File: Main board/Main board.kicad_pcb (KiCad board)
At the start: 4 copper layers, 230.2 x 100.5 mm, 80 parts, among them CN1 PA001-4P, CN2 PA001-4P, J1 TagConnect_TC2030-NL, J2 Conn_01x02_Pin, J3 Conn_01x02_Pin, J5 Connector, USB-TYPE-C-16P, J6 436500201, J7 Conn_01x04_Pin, Q1 SI7232DN-T1-GE3, Q2 SI7232DN-T1-GE3, SW1 SKRKAEE020, SW2 SKRKAEE020, U1 STM32U575VGTx, U2 TPS62901RPJR, U3 MS5607-02BA03, U4 ADXL375BCCZ-RL7, U5 SN74LVC1G32MDBVREP, U6 MMC5983MA, U9 ICM-45686, X1 1XXD32000MBA

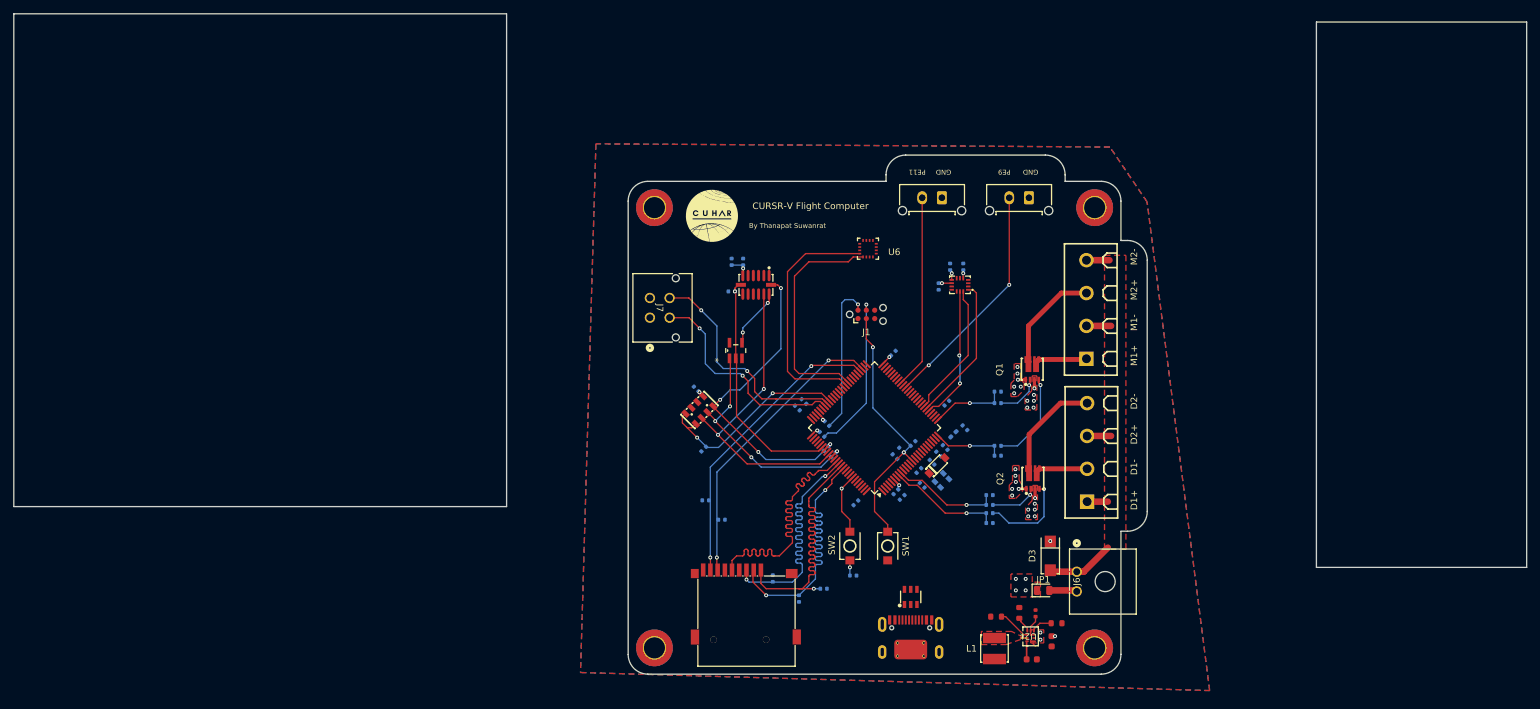
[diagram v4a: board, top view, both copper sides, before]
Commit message: Final Layout (Pre-silkscreen)
- Added  1M resistors in parallel with the igniters for static dissipation
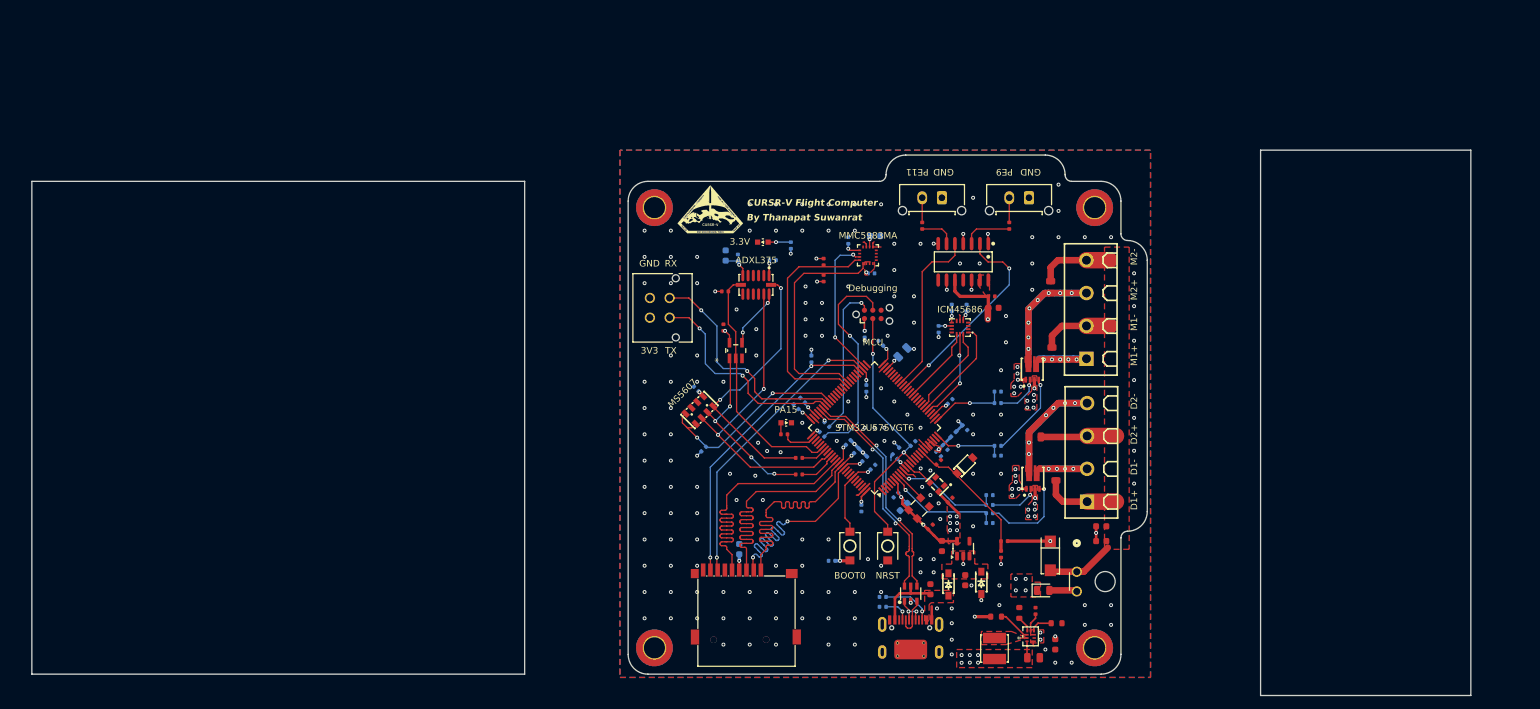
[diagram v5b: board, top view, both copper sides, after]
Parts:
- removed the G*** at (125.2, 67.8)
- added C15: 100nF, PCM_JLCPCB:C_0402, F.Cu at (167.8, 80.0)
- added C16: 100nF, PCM_JLCPCB:C_0402, B.Cu at (134.5, 74.5)
- added C22: 100nF, PCM_JLCPCB:C_0402, F.Cu at (127.0, 84.8)
- added C23: 1uF, PCM_JLCPCB:C_0402, B.Cu at (146.0, 71.5)
- added C24: 10uF, PCM_JLCPCB:C_0603, B.Cu at (150.1, 70.8)
- added C25: 10uF, PCM_JLCPCB:C_0603, F.Cu at (168.1, 81.8)
- added C26: 10uF, PCM_JLCPCB:C_0603, F.Cu at (158.5, 124.6)
- added C31: 10uF, PCM_JLCPCB:C_0603, F.Cu at (184.5, 117.2)
- added C32: 100nF, PCM_JLCPCB:C_0603, F.Cu at (184.5, 115.0)
- added C34: 4.7uF, PCM_JLCPCB:C_0805, B.Cu at (154.3, 88.5)
- added C35: 10uF, PCM_JLCPCB:C_0603, F.Cu at (160.2, 118.0)
- added C36: 10uF, PCM_JLCPCB:C_0603, F.Cu at (163.8, 123.2)
- added C37: 100nF, PCM_JLCPCB:C_0603, B.Cu at (129.4, 118.5)
- added C38: 100nF, PCM_JLCPCB:C_0402, B.Cu at (149.5, 76.5)
- added D4: GREEN, LEDDD:WL-SMCW_0603, F.Cu at (133.0, 71.8)
- added D5: Blue, LEDDD:WL-SMCW_0603, F.Cu at (136.6, 99.2)
- added G***: LOGO, LOGO, F.Cu at (125.0, 66.8)
- added G***: LOGO, LOGO, B.Cu at (133.8, 67.5)
- added G***: LOGO, LOGO, B.Cu at (145.5, 66.8)
- added G***: LOGO, LOGO, B.Cu at (124.8, 67.5)
- added R17: 4.7kΩ, PCM_JLCPCB:R_0402, F.Cu at (142.2, 77.2)
- added R18: 4.7kΩ, PCM_JLCPCB:R_0402, F.Cu at (142.2, 74.8)
- added R19: 10kΩ, PCM_JLCPCB:R_0402, B.Cu at (149.8, 106.0)
- added R20: 100Ω, PCM_JLCPCB:R_0402, B.Cu at (148.5, 85.8)
- added R21: 470Ω, PCM_JLCPCB:R_0402, B.Cu at (137.3, 72.2)
- added R22: 5.1kΩ, PCM_JLCPCB:R_0402, B.Cu at (151.2, 127.2)
- added R23: 5.1kΩ, PCM_JLCPCB:R_0402, B.Cu at (151.2, 125.8)
- added R27: 47kΩ, PCM_JLCPCB:R_0402, F.Cu at (169.8, 117.2)
- added R28: 27kΩ, PCM_JLCPCB:R_0402, F.Cu at (169.2, 119.2)
- added R39: 470Ω, PCM_JLCPCB:R_0402, F.Cu at (136.2, 101.0)
- added R40: 1MΩ, PCM_JLCPCB:R_0805, F.Cu at (176.8, 78.6)
- added R41: 1MΩ, PCM_JLCPCB:R_0805, F.Cu at (177.0, 88.7)
- added R42: 1MΩ, PCM_JLCPCB:R_0805, F.Cu at (177.6, 107.1)
- added R43: 1MΩ, PCM_JLCPCB:R_0805, F.Cu at (174.4, 101.4)
- added R5: 75Ω, PCM_JLCPCB:R_0402, F.Cu at (170.5, 69.2)
- added R8: 75Ω, PCM_JLCPCB:R_0402, F.Cu at (157.2, 69.2)
- added U10: TLV75733PDBV, Package_TO_SOT_SMD:SOT-23-5, F.Cu at (163.5, 118.4)
- added U11: NRVB120VLSFT1G, EASYEDA:SOD-123_L2.7-W1.6-LS3.7-RD-1, F.Cu at (161.2, 123.8)
- added U12: NRVB120VLSFT1G, EASYEDA:SOD-123_L2.7-W1.6-LS3.7-RD-1, F.Cu at (166.2, 123.6)
- added U7: SN74AHCT125DR, EASYEDA:SOIC-14_L8.7-W3.9-P1.27-LS6.0-BL, F.Cu at (163.5, 74.8)
- added Y1: ECS-327TXO-33-TR, LSE:OSC_ECS-327TXO-33-TR, F.Cu at (156.8, 112.2)
- C1, C21: footprint PCM_JLCPCB:C_0402 -> PCM_JLCPCB:C_0603
- C10: value 1uF -> 100nF; moved to F.Cu
- C11: value 100pF -> 100nF; moved to F.Cu
- C28: footprint PCM_JLCPCB:C_0603 -> PCM_JLCPCB:C_0805
- C30, R15, R16, R6: moved to F.Cu
- CN1, CN2: footprint EasyEDA:CONN-TH_4P-P5.08_PA001-4P -> EASYEDA:CONN-TH_4P-P5.08_PA001-4P
- Card1: footprint EasyEDA:TF-SMD_TF-015 -> EASYEDA:TF-SMD_TF-015
- D1: footprint EasyEDA:SOT-23-6_L2.9-W1.6-P0.95-LS2.8-BL -> EASYEDA:SOT-23-6_L2.9-W1.6-P0.95-LS2.8-BL
- D2: value 3V 500mW -> MMSZ4683T1G; footprint EasyEDA:SOD-123_L2.8-W1.8-LS3.7-RD -> EASYEDA:SOD-123_L2.8-W1.8-LS3.7-RD
- D3: footprint EasyEDA:SMA_L4.4-W2.6-LS5.0-RD -> EASYEDA:SMA_L4.4-W2.6-LS5.0-RD
- L1: footprint EasyEDA:IND-SMD_L4.0-W4.0 -> EASYEDA:IND-SMD_L4.0-W4.0
- Q1, Q2: footprint EasyEDA:POWER-1212-8_L3.3-W3.3-P0.66-LS3.3-BL -> EASYEDA:POWER-1212-8_L3.3-W3.3-P0.66-LS3.3-BL
- SW1, SW2: footprint EasyEDA:SW-SMD_L3.9-W3.0-P4.45 -> EASYEDA:SW-SMD_L3.9-W3.0-P4.45
- U3: footprint EasyEDA:SENSOR-SMD_MS560702BA03-50 -> EASYEDA:SENSOR-SMD_MS560702BA03-50
- U4: footprint EasyEDA:LGA-14_L5.0-W3.0-P0.80-BL -> EASYEDA:LGA-14_L5.0-W3.0-P0.80-BL
- U6: footprint EasyEDA:LGA-16_L3.0-W3.0-P0.50-BL_SQ -> EASYEDA:LGA-16_L3.0-W3.0-P0.50-BL_SQ
- U9: footprint EasyEDA:LGA-14_L3.0-W2.5-P0.50-TL -> EASYEDA:LGA-14_L3.0-W2.5-P0.50-TL
- X1: footprint EasyEDA:OSC-SMD_4P-L2.0-W1.6-BL_1XXD -> EASYEDA:OSC-SMD_4P-L2.0-W1.6-BL_1XXD; moved to F.Cu
- moved R9 29.7 mm to (148.8, 94.0), turned to -90 degrees
- moved R10 26.9 mm to (140.4, 89.5), turned to 90 degrees
- moved R13 23.7 mm to (146.0, 102.2), turned to 45 degrees
- moved R12 23.5 mm to (148.5, 104.8), turned to 45 degrees
- moved R11 21.6 mm to (147.2, 103.5), turned to 45 degrees
- moved C11 8.77 mm to (158.5, 115.1), turned to 45 degrees
- moved R31 6.50 mm to (159.8, 85.0)
- moved U9 6.50 mm to (163.0, 84.8)
- moved C10 6.37 mm to (161.5, 111.0), turned to 45 degrees
- moved C17 6.27 mm to (164.0, 81.8)
- moved C19 6.25 mm to (161.8, 81.8)
- moved R16 6.05 mm to (138.5, 107.1), turned to 0 degrees
- moved R15 4.39 mm to (138.5, 104.6), turned to 0 degrees
- moved C30 4.30 mm to (159.8, 105.2), turned to 45 degrees
- moved D2 4.25 mm to (163.8, 105.8)
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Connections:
- C11 pad 1: Net-(X1-Output) -> +3V3
- C11 pad 2: HSE_IN -> VBAT-
- J1 pad 1: +3V3 -> Net-(J1-VCC)
- J2 pad 2: PWM1 -> SERVO1
- J3 pad 2: PWM2 -> SERVO2
- J5 pad A12B1: Net-(J5-GND-PadA12B1) -> VBAT-
- J5 pad B12A1: Net-(J5-GND-PadA12B1) -> VBAT-
- SW2 pad 1: +3V3 -> /Boot0
- SW2 pad 2: VBAT- -> +3V3
- U1 pad 15: BAT_LEVEL -> unconnected-(U1-PC0-Pad15)
- U1 pad 18: unconnected-(U1-PC3-Pad18) -> BAT_LEVEL
- U1 pad 37: unconnected-(U1-PB2-Pad37) -> ICM_CS
- U1 pad 52: unconnected-(U1-PB13-Pad52) -> MMC_INT
- U1 pad 7: unconnected-(U1-PC13-Pad7) -> FIRE_D
- U1 pad 77: unconnected-(U1-PA15-Pad77) -> PA15
- U1 pad 8: FIRE_D -> LSE_IN
- U1 pad 94: VBAT- -> /Boot0
- X1 pad 3: Net-(X1-Output) -> HSE_IN
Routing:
- net +3V3: track 13.1 -> 91.6 mm, vias 7 -> 37
- net +5V: track 2.77 -> 58.1 mm, vias 0 -> 9
- net USB_DN: track 0.00 -> 34.9 mm, vias 0 -> 2
- net USB_DP: track 0.00 -> 34.9 mm, vias 0 -> 2
- net PYRO+: track 24.4 -> 56.2 mm
- net MMC_INT: track 0.00 -> 22.3 mm, vias 0 -> 2
- net BAT_LEVEL: track 0.00 -> 21.1 mm
- net VBAT-: track 14.3 -> 34.5 mm, vias 1 -> 175
- net Net-(CN1-Pad3): track 17.1 -> 35.1 mm, vias 0 -> 8
- net Net-(CN2-Pad4): track 17.0 -> 33.0 mm, vias 0 -> 6
- net /Boot0: track 0.00 -> 12.3 mm, vias 0 -> 1
- net ICM_CS: track 0.00 -> 12.0 mm
- net VBUS: track 0.00 -> 10.2 mm
- net Net-(J1-SWCLK): track 24.4 -> 32.5 mm
- net Net-(J5-CC2): track 0.00 -> 7.95 mm, vias 0 -> 1
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- added copper zone on F.Cu, net +3.3VA
- added copper zone on F.Cu, net +3V3
- added copper zone on In2.Cu, net +3V3
- added copper zone on F.Cu, net +5V
- added copper zone on In2.Cu, net +5V
- added copper zone on F.Cu, net Net-(U10-EN)
- added copper zone on F.Cu, net VBUS
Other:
- board size 230.2 x 100.5 mm -> 219 x 83 mm
- board text added: "3.3V"
- board text added: "3V3"
- board text added: "ADXL375"
- board text added: "BOOT0"
- board text added: "Debugging"
- board text added: "ICM45686"
- board text added: "MCU"
- board text added: "MMC5983MA"
- board text added: "MS5607"
- board text added: "NRST"
- board text added: "PA15"
- board text added: "RX"
- board text added: "STM32U575VGT6"
- board text added: "TX"

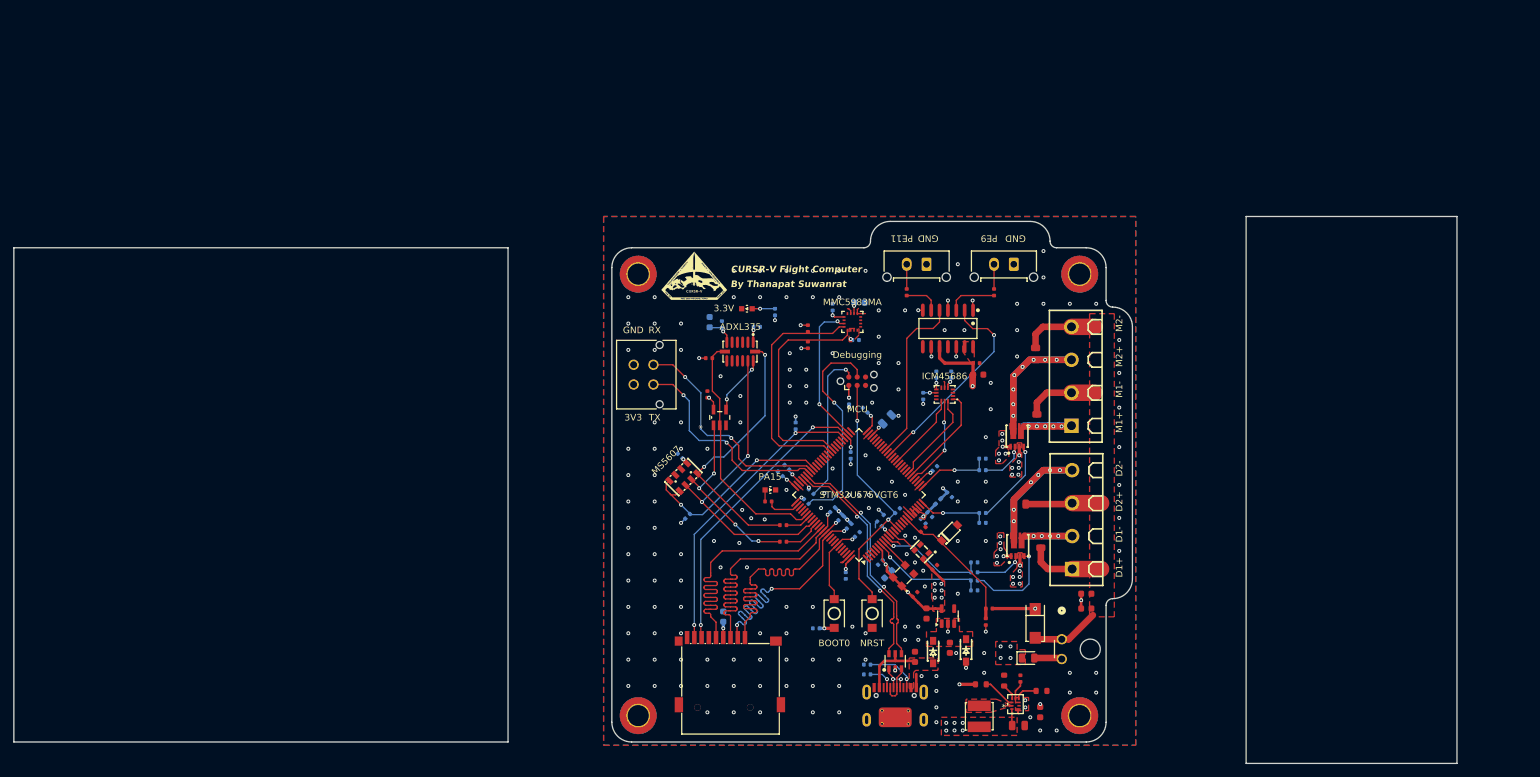
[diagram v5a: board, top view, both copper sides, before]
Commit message: Minor Adjustment + Silkscreen
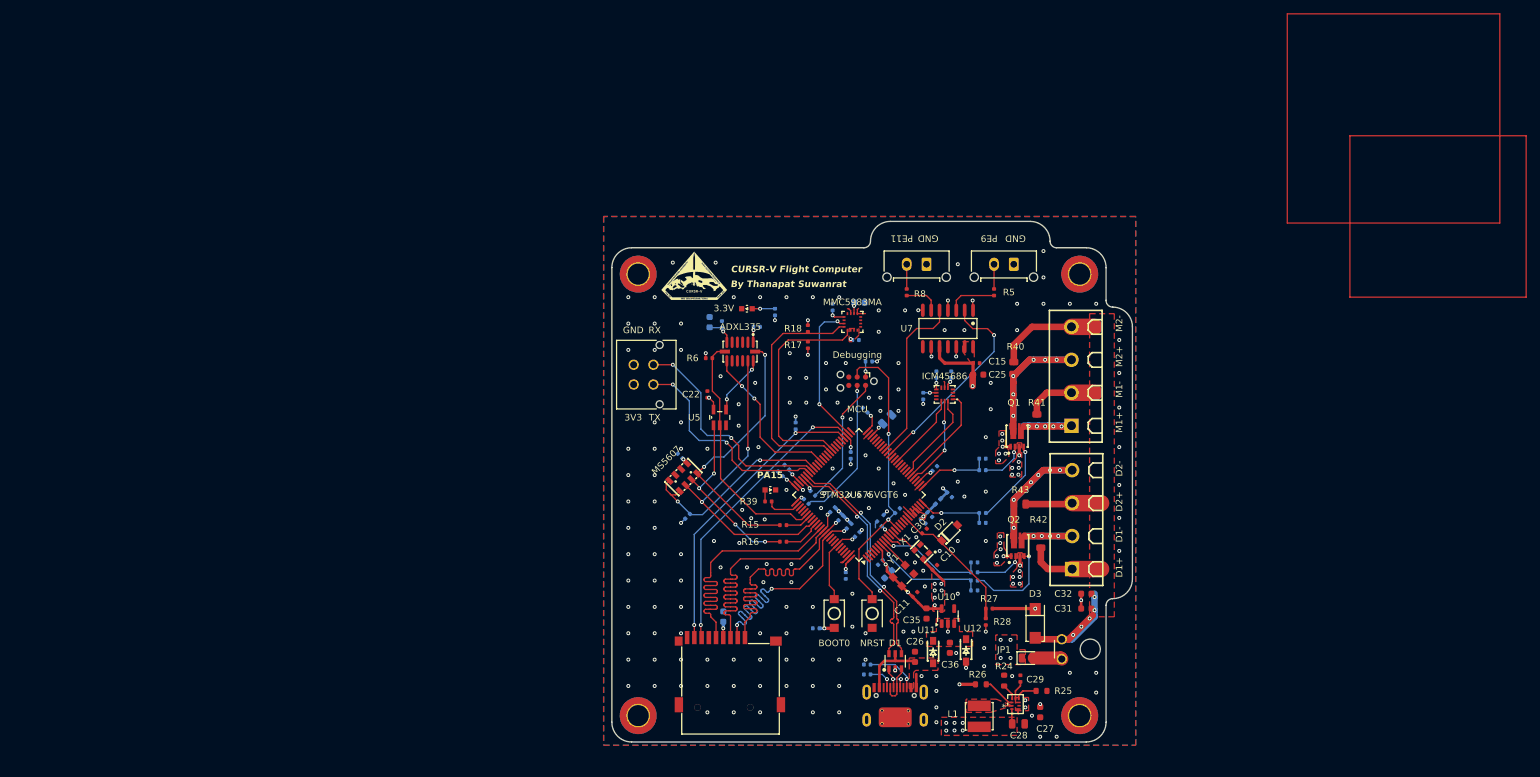
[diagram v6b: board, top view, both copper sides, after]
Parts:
- moved R20 6.71 mm to (151.5, 79.8), turned to 180 degrees
- moved R40 3.94 mm to (173.5, 80.8)
- moved G*** 0.79 mm to (146.2, 67.0)
- moved G*** 0.35 mm to (134.0, 67.8)
- moved R4 0.35 mm to (143.0, 99.8)
- moved C30 0.29 mm to (159.9, 105.5)
- moved C28 0.25 mm to (174.2, 134.8)
- turned J1 to 180 degrees
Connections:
- U1 pad 64: unconnected-(U1-PC7-Pad64) -> ADXL_INT1
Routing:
- net ADXL_INT1: track 0.00 -> 24.4 mm, vias 0 -> 2
- net PYRO+: track 56.2 -> 70.6 mm, vias 0 -> 5
- net Net-(J1-SWCLK): track 32.5 -> 22.2 mm
- net nRST: track 39.8 -> 45.7 mm
- net Net-(J1-SWDIO): track 23.2 -> 19.9 mm
- net VBAT-: track 34.5 -> 35.4 mm, vias 175 -> 178
- net +3V3: track 91.6 -> 91.0 mm
- net Net-(CN1-Pad3): vias 8 -> 6
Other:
- board size 219 x 83 mm -> 79 x 79 mm
- board text added: "C1"
- board text added: "C10"
- board text added: "C11"
- board text added: "C12"
- board text added: "C13"
- board text added: "C14"
- board text added: "C15"
- board text added: "C16"
- board text added: "C17"
- board text added: "C18"
- board text added: "C19"
- board text added: "C2"
- board text added: "C20"
- board text added: "C21"
- board text added: "C22"
- board text added: "C23"
- board text added: "C24"
- board text added: "C25"
- board text added: "C26"
- board text added: "C27"
- board text added: "C28"
- board text added: "C29"
- board text added: "C3"
- board text added: "C30"
- board text added: "C31"
- board text added: "C32"
- board text added: "C34"
- board text added: "C35"
- board text added: "C36"
- board text added: "C37"
- board text added: "C38"
- board text added: "C4"
- board text added: "C5"
- board text added: "C6"
- board text added: "C7"
- board text added: "C8"
- board text added: "C9"
- board text added: "D1"
- board text added: "D2"
- board text added: "D3"
- board text added: "FB1"
- board text added: "JP1"
- board text added: "L1"
- board text added: "Q1"
- board text added: "Q2"
- board text added: "R1"
- board text added: "R10"
- board text added: "R11"
- board text added: "R12"
- board text added: "R13"
- board text added: "R14"
- board text added: "R15"
- board text added: "R16"
- board text added: "R17"
- board text added: "R18"
- board text added: "R19"
- board text added: "R2"
- board text added: "R20"
- board text added: "R21"
- board text added: "R22"
- board text added: "R23"
- board text added: "R24"
- board text added: "R25"
- board text added: "R26"
- board text added: "R27"
- board text added: "R28"
- board text added: "R3"
- board text added: "R31"
- board text added: "R32"
- board text added: "R33"
- board text added: "R34"
- board text added: "R35"
- board text added: "R36"
- board text added: "R37"
- board text added: "R38"
- board text added: "R39"
- board text added: "R4"
- board text added: "R40"
- board text added: "R41"
- board text added: "R42"
- board text added: "R43"
- board text added: "R5"
- board text added: "R6"
- board text added: "R7"
- board text added: "R8"
- board text added: "R9"
- board text added: "U10"
- board text added: "U11"
- board text added: "U12"
- board text added: "U5"
- board text added: "U7"
- board text added: "X1"
- board text added: "Y1"
